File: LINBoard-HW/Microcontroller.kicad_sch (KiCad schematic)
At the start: 43 parts, among them J1 DEBUG, SW2 RESET, SW3 BOOT, U1 RP2350_60QFN, U5 W25Q128JVS, Y1 ABM8-272-T3

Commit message: board layout started
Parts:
- removed C18: 1uF, Capacitor_SMD:C_0603_1608Metric, symbol Device:C_Small
- C10, C11, C12, C13, C14, C15, C16, C17, C19, C22, C23, C6, C7, C8, C9: footprint Capacitor_SMD:C_0603_1608Metric -> Capacitor_SMD:C_0402_1005Metric
- C20, C21: footprint Capacitor_SMD:C_0603_1608Metric -> RP2350_60QFN_minimal:C_0402_1005Metric_small_pads
- D5, D8, D9: footprint LED_SMD:LED_0805_2012Metric -> LED_SMD:LED_0603_1608Metric
- J1: symbol Connector_Generic:Conn_01x03 -> Connector_Generic_MountingPin:Conn_01x03_MountingPin
- R10, R11, R12, R15, R16, R20, R3, R5, R6, R7, R8, R9: footprint Resistor_SMD:R_0603_1608Metric -> Resistor_SMD:R_0402_1005Metric
- SW2, SW3: footprint Button_Switch_SMD:SW_Push_1P1T_NO_Vertical_Wuerth_434133025816 -> Buttons:TS-1088-AR02016
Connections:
- net GND: now also J1.MP (MountPin)
- net ENABLE: no longer names the net of U1.13 (GPIO9)
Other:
- note removed: "PIN44"

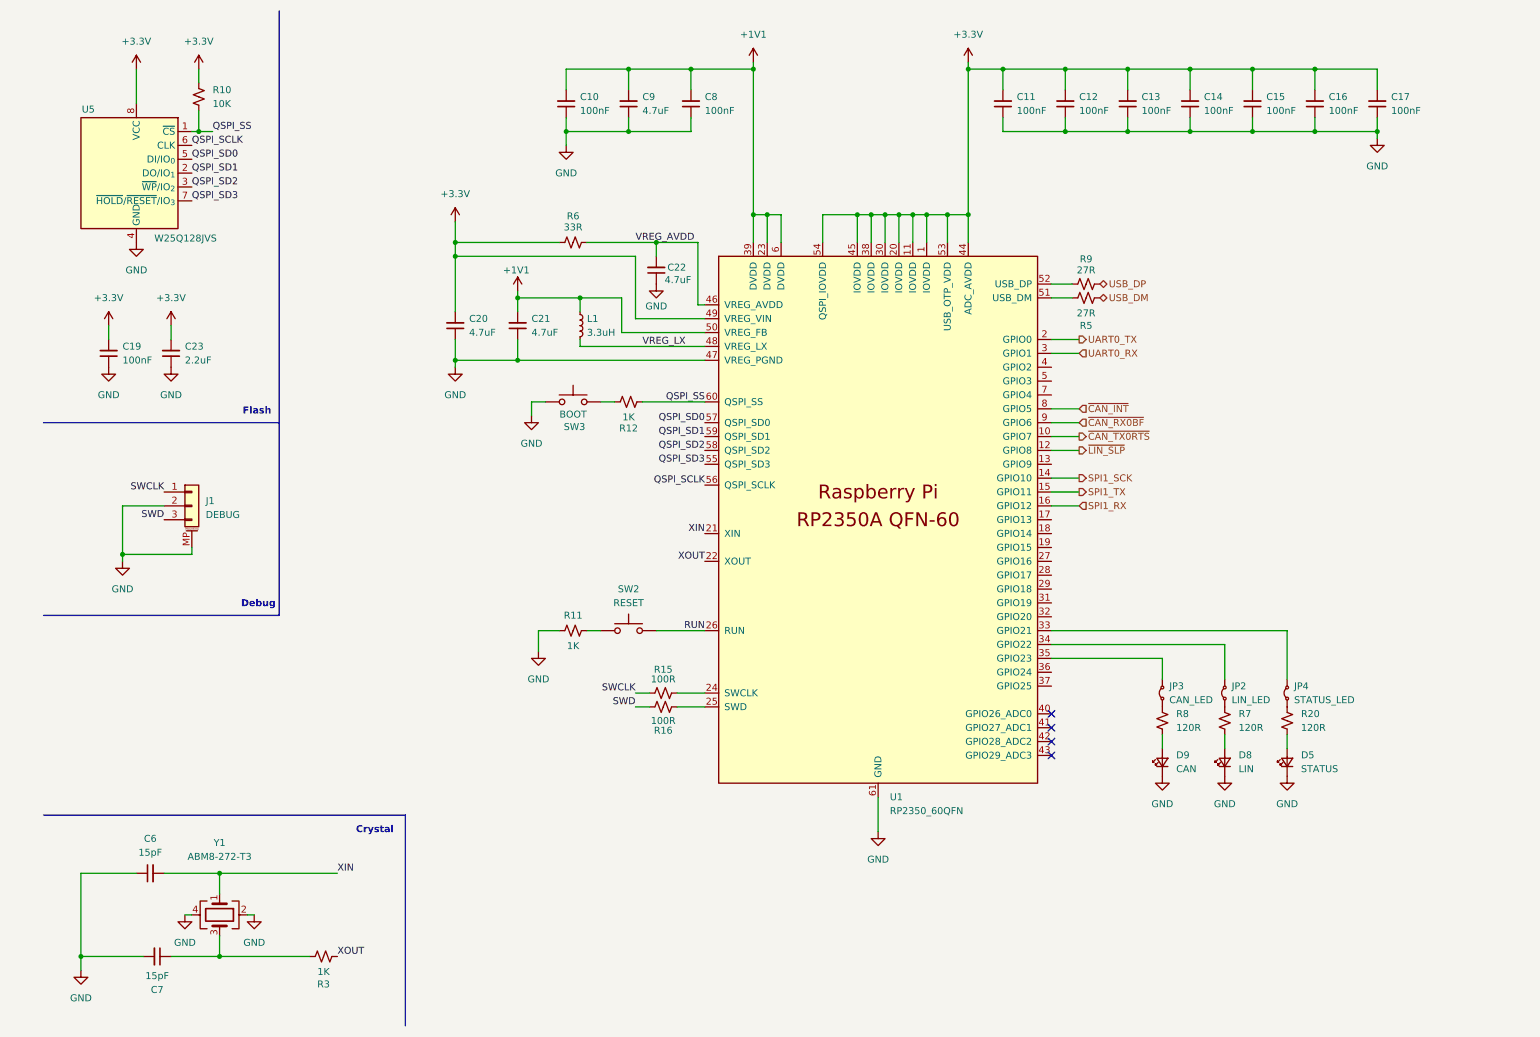
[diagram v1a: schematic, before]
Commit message: change usb
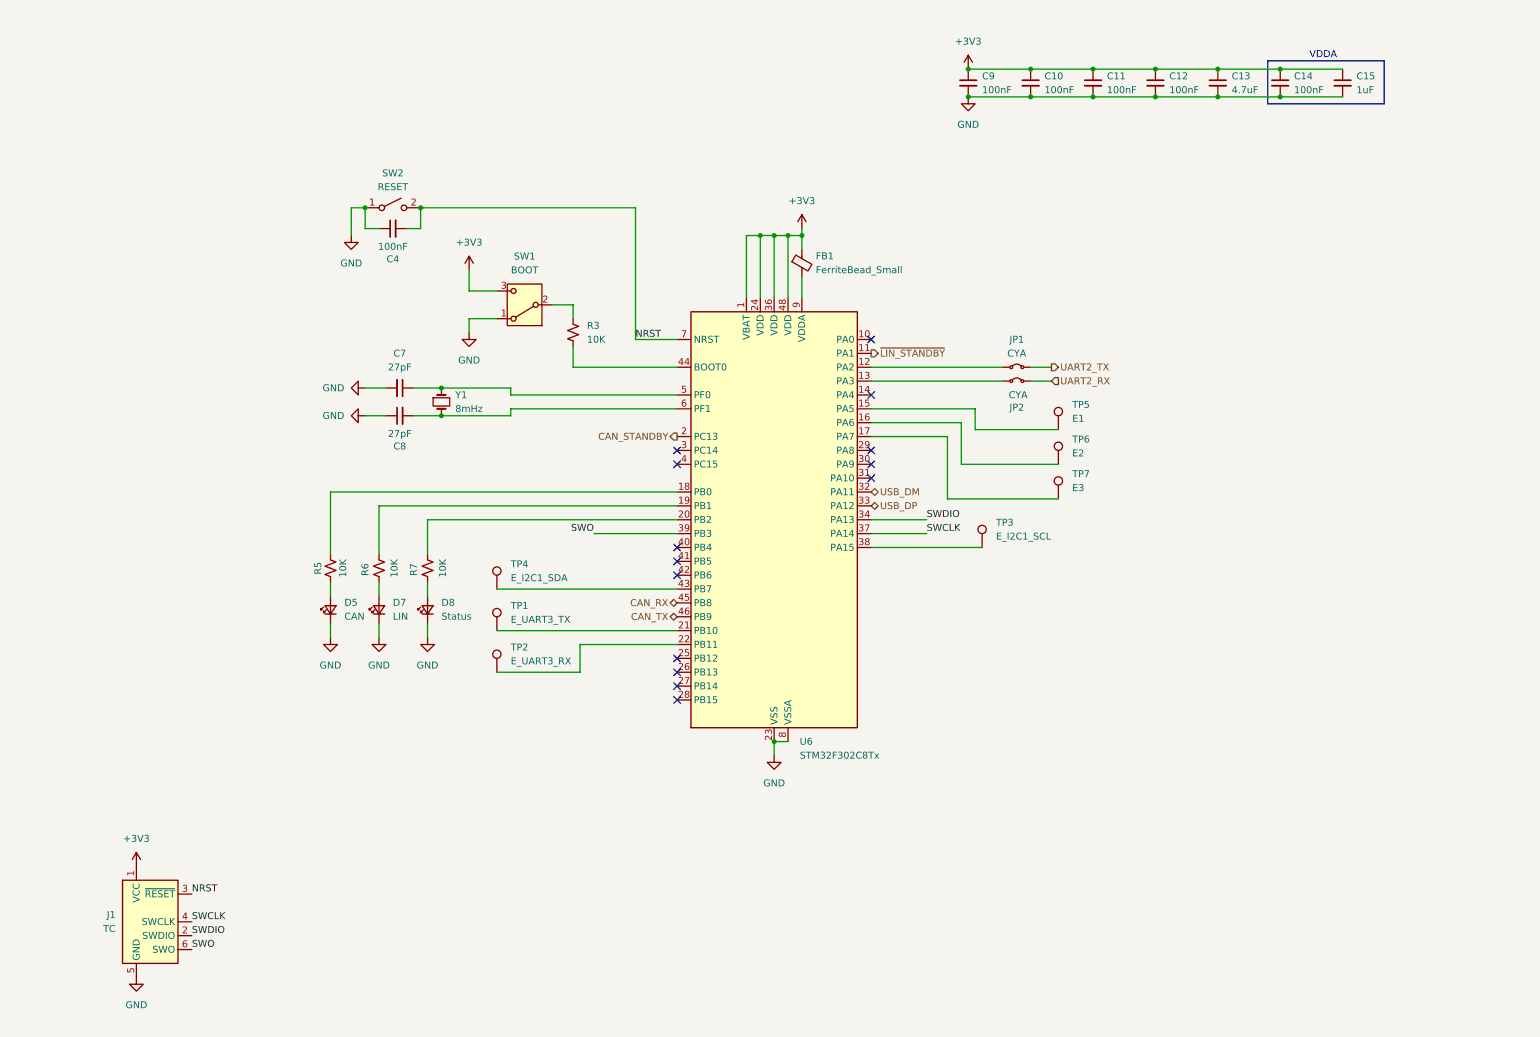
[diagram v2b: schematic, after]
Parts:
- removed C16, C17, C19: 100nF, Capacitor_SMD:C_0402_1005Metric, symbol Device:C_Small
- removed C20, C21: 4.7uF, RP2350_60QFN_minimal:C_0402_1005Metric_small_pads, symbol Device:C_Small
- removed C22: 4.7uF, Capacitor_SMD:C_0402_1005Metric, symbol Device:C_Small
- removed C23: 2.2uF, Capacitor_SMD:C_0402_1005Metric, symbol Device:C_Small
- removed C6: 15pF, Capacitor_SMD:C_0402_1005Metric, symbol Device:C_Small
- removed D9: CAN, LED_SMD:LED_0603_1608Metric, symbol Device:LED_Small
- removed J1: DEBUG, Connector_JST:JST_SH_SM03B-SRSS-TB_1x03-1MP_P1.00mm_Horizontal, symbol Connector_Generic_MountingPin:Conn_01x03_MountingPin
- removed JP3: CAN_LED, Jumper:SolderJumper-2_P1.3mm_Bridged_RoundedPad1.0x1.5mm, symbol Jumper:Jumper_2_Small_Bridged
- removed JP4: STATUS_LED, Jumper:SolderJumper-2_P1.3mm_Bridged_RoundedPad1.0x1.5mm, symbol Jumper:Jumper_2_Small_Bridged
- removed L1: 3.3uH, RP2350_60QFN_minimal:L_pol_2016, symbol Device:L_Small
- removed R10: 10K, Resistor_SMD:R_0402_1005Metric, symbol Device:R_Small_US
- removed R11, R12: 1K, Resistor_SMD:R_0402_1005Metric, symbol Device:R_Small_US
- removed R15, R16: 100R, Resistor_SMD:R_0402_1005Metric, symbol Device:R_Small_US
- removed R20, R8: 120R, Resistor_SMD:R_0402_1005Metric, symbol Device:R_Small_US
- removed R9: 27R, Resistor_SMD:R_0402_1005Metric, symbol Device:R_Small_US
- removed SW2: RESET, Buttons:TS-1088-AR02016, symbol Switch:SW_Push
- removed SW3: BOOT, Buttons:TS-1088-AR02016, symbol Switch:SW_Push
- removed U1: RP2350_60QFN, RP2350_60QFN_minimal:RP2350-QFN-60-1EP_7x7_P0.4mm_EP3.4x3.4mm_ThermalVias, symbol RaspberryPi:RP2350_60QFN
- removed U5: W25Q128JVS, Package_SO:SOIC-8_5.3x5.3mm_P1.27mm, symbol Memory_Flash:W25Q128JVS
- removed Y1: ABM8-272-T3, Crystal:Crystal_SMD_3225-4Pin_3.2x2.5mm, symbol Device:Crystal_GND24
- added C4: 100nF, Capacitor_SMD:C_0402_1005Metric, symbol Device:C_Small
- added D7: LIN, LED_SMD:LED_0603_1608Metric, symbol Device:LED_Small
- added FB1: FerriteBead_Small, Resistor_SMD:R_0402_1005Metric, symbol Device:FerriteBead_Small
- added J1: TC, Connector:Tag-Connect_TC2030-IDC-NL_2x03_P1.27mm_Vertical, symbol Connector:Conn_ARM_SWD_TagConnect_TC2030-NL
- added JP1: CYA, Jumper:SolderJumper-2_P1.3mm_Bridged2Bar_RoundedPad1.0x1.5mm, symbol Jumper:Jumper_2_Small_Bridged
- added SW1: BOOT, SlideSwitch:CJS-1200TB, symbol Switch:SW_SPDT
- added SW2: RESET, switch_pb:SW-SMD_4P-L5.1-W5.1-P3.70-LS6.5-TL_H1.5, symbol Switch:SW_SPST
- added TP1: E_UART3_TX, TestPoint:TestPoint_Keystone_5000-5004_Miniature, symbol Connector:TestPoint
- added TP2: E_UART3_RX, TestPoint:TestPoint_Keystone_5000-5004_Miniature, symbol Connector:TestPoint
- added TP3: E_I2C1_SCL, TestPoint:TestPoint_Keystone_5000-5004_Miniature, symbol Connector:TestPoint
- added TP4: E_I2C1_SDA, TestPoint:TestPoint_Keystone_5000-5004_Miniature, symbol Connector:TestPoint
- added TP5: E1, TestPoint:TestPoint_Keystone_5000-5004_Miniature, symbol Connector:TestPoint
- added TP6: E2, TestPoint:TestPoint_Keystone_5000-5004_Miniature, symbol Connector:TestPoint
- added TP7: E3, TestPoint:TestPoint_Keystone_5000-5004_Miniature, symbol Connector:TestPoint
- added U6: STM32F302C8Tx, Package_QFP:LQFP-48_7x7mm_P0.5mm, symbol MCU_ST_STM32F3:STM32F302C8Tx
- added Y1: 8mHz, Crystals_Modify:Crystal_SMD_5032-2Pin_5.0x3.2mm_HandSoldering, symbol Device:Crystal_Small
- C13: value 100nF -> 4.7uF
- C15: value 100nF -> 1uF
- C7: value 15pF -> 27pF
- C8: value 100nF -> 27pF
- C9: value 4.7uF -> 100nF
- D5: value STATUS -> CAN
- D8: value LIN -> Status
- JP2: value LIN_LED -> CYA; footprint Jumper:SolderJumper-2_P1.3mm_Bridged_RoundedPad1.0x1.5mm -> Jumper:SolderJumper-2_P1.3mm_Bridged2Bar_RoundedPad1.0x1.5mm
- R3: value 1K -> 10K
- R5: value 27R -> 10K
- R6: value 33R -> 10K
- R7: value 120R -> 10K
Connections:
- net GND: now also C10.2, C11.2, C12.2, C13.2, C14.2, C15.2, C9.2, C4.1, D7.1 (K), J1.5 (GND), SW1.1 (A), SW2.1 (A), U6.23 (VSS), U6.35 (VSS), U6.47 (VSS), U6.8 (VSSA); no longer C10.1, C11.1, C12.1, C13.1, C14.1, C15.1, C9.1
- net SWCLK: now also J1.4 (SWCLK), U6.37 (PA14)
- net USB_DM: now also U6.32 (PA11); no longer R5.1
- net USB_DP: now also U6.33 (PA12)
- net at C7.1: now also U6.5 (PF0), Y1.1; no longer R3.2
- net at R7.1: now also U6.20 (PB2); no longer JP2.1 (A)
- net UART2_RX: now reaches JP2.2 (B)
- net at D5.2 (A): now also R5.2
- removed net +1V1: C10.2, C8.2, C9.2
- removed net +3.3V: C11.2, C12.2, C13.2, C14.2, C15.2, R6.1
- net VREG_AVDD: no longer names the net of R6.2
- net VREG_AVDD: now also D7.2 (A)
- net XOUT: no longer names the net of R3.1
- net XOUT: now also U6.44 (BOOT0)
- new net: TP5.1, U6.15 (PA5)
- new net: TP7.1, U6.17 (PA7)
- new net: C8.2, U6.6 (PF1), Y1.2
- new net: JP1.1 (A), U6.12 (PA2)
- new net: R3.2, SW1.2 (B)
- new net: TP4.1, U6.43 (PB7)
- new net: R5.1, U6.18 (PB0)
- new net: TP1.1, U6.21 (PB10)
- new net: TP6.1, U6.16 (PA6)
- new net: JP2.1 (A), U6.13 (PA3)
- new net: R6.1, U6.19 (PB1)
- new net: FB1.2, U6.9 (VDDA)
- new net: TP3.1, U6.38 (PA15)
- new net: TP2.1, U6.22 (PB11)
- new net +3V3: C10.1, C11.1, C12.1, C13.1, C14.1, C15.1, C9.1, FB1.1, J1.1 (VCC), SW1.3 (C), U6.1 (VBAT), U6.24 (VDD), U6.36 (VDD), U6.48 (VDD)
- new net CAN_RX: U6.45 (PB8)
- new net CAN_STANDBY: U6.2 (PC13)
- new net CAN_TX: U6.46 (PB9)
- new net NRST: C4.2, J1.3 (~{RESET}), SW2.2 (B), U6.7 (NRST)
- new net SWDIO: J1.2 (SWDIO), U6.34 (PA13)
- new net SWO: J1.6 (SWO), U6.39 (PB3)
- new net UART2_TX: JP1.2 (B)
- new net ~{LIN_STANDBY}: U6.11 (PA1)
- no-connect marks 4 -> 14
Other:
- note added: "VDDA"
- note removed: "Crystal"
- note removed: "Debug"
- note removed: "Flash"

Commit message: doing some layout
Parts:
- removed C15: 1uF, Capacitor_SMD:C_0402_1005Metric, symbol Device:C_Small
- removed FB1: FerriteBead_Small, Resistor_SMD:R_0402_1005Metric, symbol Device:FerriteBead_Small
- C10, C11, C4, C7, C8, C9: footprint Capacitor_SMD:C_0402_1005Metric -> Capacitor_SMD:C_0805_2012Metric
- C12: value 100nF -> 4.7uF; footprint Capacitor_SMD:C_0402_1005Metric -> Capacitor_SMD:C_0805_2012Metric
- C13: value 4.7uF -> 10nF; footprint Capacitor_SMD:C_0402_1005Metric -> Capacitor_SMD:C_0805_2012Metric
- C14: value 100nF -> 1uF; footprint Capacitor_SMD:C_0402_1005Metric -> Capacitor_SMD:C_0805_2012Metric
- D5, D7, D8: footprint LED_SMD:LED_0603_1608Metric -> LED_SMD:LED_0805_2012Metric
- R3, R5, R6, R7: footprint Resistor_SMD:R_0402_1005Metric -> Resistor_SMD:R_0805_2012Metric
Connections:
- net +3V3: now also U6.9 (VDDA)

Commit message: routing first pass complete
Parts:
- added C5: 100nF, Capacitor_SMD:C_0805_2012Metric, symbol Device:C_Small
- added R8, R9: 10K, Resistor_SMD:R_0805_2012Metric, symbol Device:R_Small_US
- added U5: MB85RC256V, Package_SO:SOIC-8_3.9x4.9mm_P1.27mm, symbol Memory_FRAM:MB85RC256V
- TP3: value E_I2C1_SCL -> SDA
- TP4: value E_I2C1_SDA -> SCL
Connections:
- net GND: now also C5.2, U5.1 (A0), U5.2 (A1), U5.3 (A2), U5.4 (VSS), U5.7 (WP)
- net I2C1_SCL: now reaches TP4.1
- net I2C1_SCL: now also U6.38 (PA15), R9.2, U5.6 (SCL); no longer U6.43 (PB7)
- net I2C1_SDA: now reaches TP3.1
- net I2C1_SDA: now also U6.43 (PB7), R8.2, U5.5 (SDA); no longer U6.38 (PA15)
- net +3V3 renamed +3.3V
- net +3.3V: now also C5.1, R8.1, R9.1, U5.8 (VDD)
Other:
- note added: "I2C1 ADDR 0x50"

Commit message: add fab outputs
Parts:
- C10, C11, C4, C5, C9: LCSC Part (none) -> C49678
- C12: LCSC Part (none) -> C1779
- C13: LCSC Part (none) -> C1710
- C14: LCSC Part (none) -> C28323
- C7, C8: LCSC Part (none) -> C1808
- D5, D7: LCSC Part (none) -> C2296
- D8: LCSC Part (none) -> C2297
- JP1, JP2, SW1, TP1, TP2, TP3, TP4, TP5, TP6, TP7: now left out of the parts list
- R3, R5, R6, R7, R8, R9: LCSC Part (none) -> C17414
- SW2: LCSC Part (none) -> C318884
- U5: LCSC Part (none) -> C47538
- U6: value STM32F302C8Tx -> STM32F302CCTx; LCSC Part (none) -> C262946
- Y1: LCSC Part (none) -> C144380

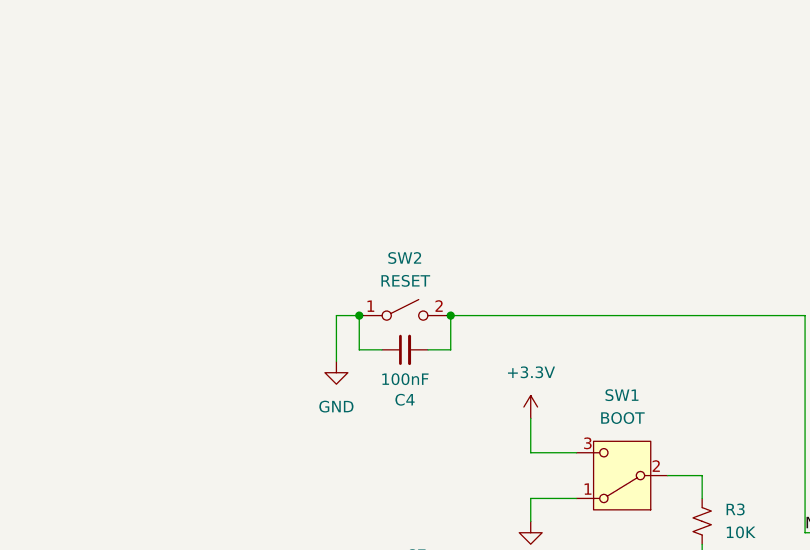
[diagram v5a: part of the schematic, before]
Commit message: add tvs, fix reset button
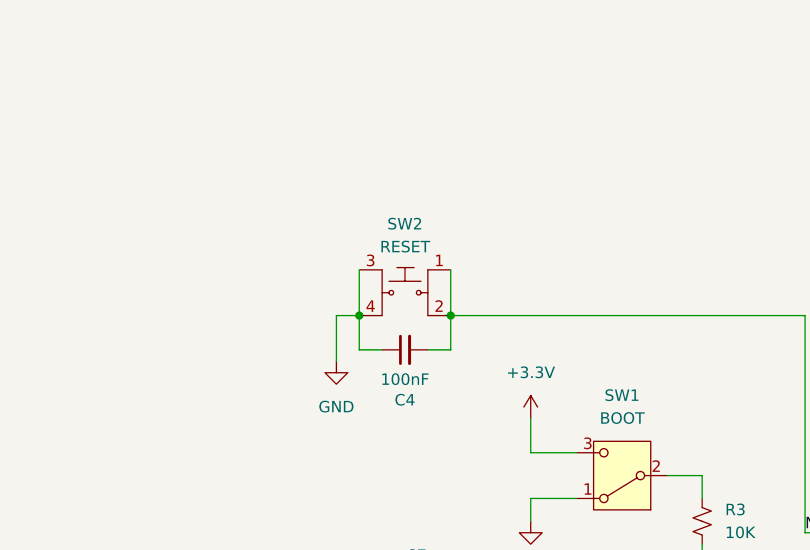
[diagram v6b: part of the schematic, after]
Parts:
- SW2: symbol Switch:SW_SPST -> dk_Tactile-Switches:1825910-6; Category (none) -> Switches; Family (none) -> Tactile Switches
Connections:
- net GND: now also SW2.3, SW2.4; no longer SW2.1 (A)
- net NRST: now also SW2.1
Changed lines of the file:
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@@
+	)
+	(junction
+		(at 245.11 139.7)
+		(diameter 0)
+		(color 0 0 0 0)
+	)
+	(junction
+		(at 71.12 48.26)
+		(diameter 0)
+		(color 0 0 0 0)
+	)
+	(junction
+		(at 204.47 27.94)
+		(diameter 0)
+		(color 0 0 0 0)
+	)
+	(junction
+		(at 181.61 27.94)
+		(diameter 0)
+		(color 0 0 0 0)
+	)
+	(junction
+		(at 193.04 22.86)
+		(diameter 0)
+		(color 0 0 0 0)
+	)
+	(junction
+		(at 260.35 151.13)
+		(diameter 0)
+		(color 0 0 0 0)
+	)
+	(junction
+		(at 246.38 118.11)
+		(diameter 0)
+		(color 0 0 0 0)
+	)
+	(junction
+		(at 245.11 137.16)
+		(diameter 0)
+		(color 0 0 0 0)
+	)
+	(junction
+		(at 246.38 130.81)
+		(diameter 0)
+		(color 0 0 0 0)
+	)
+	(junction
+		(at 193.04 27.94)
+		(diameter 0)
+		(color 0 0 0 0)
+	)
+	(junction
+		(at 245.11 144.78)
+		(diameter 0)
+		(color 0 0 0 0)
+	)
+	(junction
+		(at 260.35 118.11)
+		(diameter 0)
+		(color 0 0 0 0)
 	)
 	(junction
@@
 	)
 	(junction
-		(at 245.11 139.7)
-		(diameter 0)
-		(color 0 0 0 0)
-	)
-	(junction
-		(at 204.47 27.94)
-		(diameter 0)
-		(color 0 0 0 0)
-	)
-	(junction
-		(at 181.61 27.94)
-		(diameter 0)
-		(color 0 0 0 0)
-	)
-	(junction
-		(at 193.04 22.86)
-		(diameter 0)
-		(color 0 0 0 0)
-	)
-	(junction
-		(at 260.35 151.13)
-		(diameter 0)
-		(color 0 0 0 0)
-	)
-	(junction
-		(at 246.38 118.11)
-		(diameter 0)
-		(color 0 0 0 0)
-	)
-	(junction
-		(at 245.11 137.16)
-		(diameter 0)
-		(color 0 0 0 0)
-	)
-	(junction
-		(at 246.38 130.81)
-		(diameter 0)
-		(color 0 0 0 0)
-	)
-	(junction
-		(at 193.04 27.94)
-		(diameter 0)
-		(color 0 0 0 0)
-	)
-	(junction
-		(at 245.11 144.78)
-		(diameter 0)
-		(color 0 0 0 0)
-	)
-	(junction
-		(at 260.35 118.11)
-		(diameter 0)
-		(color 0 0 0 0)
-	)
-	(junction
-		(at 71.12 48.26)
-		(diameter 0)
-		(color 0 0 0 0)
-	)
-	(junction
 		(at 151.13 60.96)
 		(diameter 0)
@@
 	(wire
 		(pts
+			(xy 71.12 43.18) (xy 71.12 48.26)
+		)
+		(stroke
+			(width 0)
+			(type default)
+		)
+	)
+	(wire
+		(pts
 			(xy 81.28 52.07) (xy 81.28 48.26)
 		)
@@
 		(pts
 			(xy 73.66 52.07) (xy 71.12 52.07)
+		)
+		(stroke
+			(width 0)
+			(type default)
+		)
+	)
+	(wire
+		(pts
+			(xy 81.28 43.18) (xy 81.28 48.26)
 		)
 		(stroke
@@
 	)
 	(symbol
-		(lib_id "Switch:SW_SPST")
-		(at 76.2 48.26 0)
+		(lib_id "dk_Tactile-Switches:1825910-6")
+		(at 76.2 45.72 0)
+		(mirror y)
 		(unit 1)
 		(exclude_from_sim no)
@@
 		(on_board yes)
 		(dnp no)
-		(fields_autoplaced yes)
 		(property "Reference" "SW2"
-			(at 76.2 41.91 0)
+			(at 76.2 38.1 0)
 			(effects
 				(font
@@
 		)
 		(property "Value" "RESET"
-			(at 76.2 44.45 0)
+			(at 76.2 40.64 0)
 			(effects
 				(font
@@
 		)
 		(property "Footprint" "switch_pb:SW-SMD_4P-L5.1-W5.1-P3.70-LS6.5-TL_H1.5"
-			(at 76.2 48.26 0)
+			(at 71.12 40.64 0)
+			(effects
+				(font
+					(size 1.524 1.524)
+				)
+				(justify left)
+				(hide yes)
+			)
+		)
+		(property "Datasheet" ""
+			(at 71.12 38.1 0)
+			(effects
+				(font
+					(size 1.524 1.524)
+				)
+				(justify left)
+				(hide yes)
+			)
+		)
+		(property "Description" ""
+			(at 76.2 45.72 0)
 			(effects
 				(font
@@
 			)
 		)
-		(property "Datasheet" "~"
-			(at 76.2 48.26 0)
+		(property "LCSC Part" "C318884"
+			(at 76.2 45.72 0)
 			(effects
 				(font
@@
 			)
 		)
-		(property "Description" "Single Pole Single Throw (SPST) switch"
-			(at 76.2 48.26 0)
-			(effects
-				(font
-					(size 1.27 1.27)
-				)
+		(property "MPN" ""
+			(at 71.12 33.02 0)
+			(effects
+				(font
+					(size 1.524 1.524)
+				)
+				(justify left)
 				(hide yes)
 			)
 		)
-		(property "LCSC Part" "C318884"
-			(at 76.2 48.26 0)
-			(effects
-				(font
-					(size 1.27 1.27)
-				)
+		(property "Category" "Switches"
+			(at 71.12 30.48 0)
+			(effects
+				(font
+					(size 1.524 1.524)
+				)
+				(justify left)
 				(hide yes)
 			)
 		)
+		(property "Family" "Tactile Switches"
+			(at 71.12 27.94 0)
+			(effects
+				(font
+					(size 1.524 1.524)
+				)
+				(justify left)
+				(hide yes)
+			)
+		)
 		(pin "2"
 		)
 		(pin "1"
 		)
+		(pin "4"
+		)
+		(pin "3"
+		)
 		(instances
